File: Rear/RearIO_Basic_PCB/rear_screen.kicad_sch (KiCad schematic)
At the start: 46 parts, among them J1 Conn_01x02_Pin, J2 Conn_01x02_Pin, J3 Conn_01x02_Pin, J4 Conn_01x02_Pin, J5 Conn_01x02_Pin, J6 Conn_01x02_Pin, J7 Conn_01x08_Socket, Q1 NTMFS4C03N-HXY, Q2 NTMFS4C03N-HXY, Q3 NTMFS4C03N-HXY, Q4 NTMFS4C03N-HXY, Q6 NTMFS4C03N-HXY, Q7 NTMFS4C03N-HXY, U1 MIC4426, U2 MIC4426, U3 AOZ1280CI, U4 ACS711xEXLT-31AB

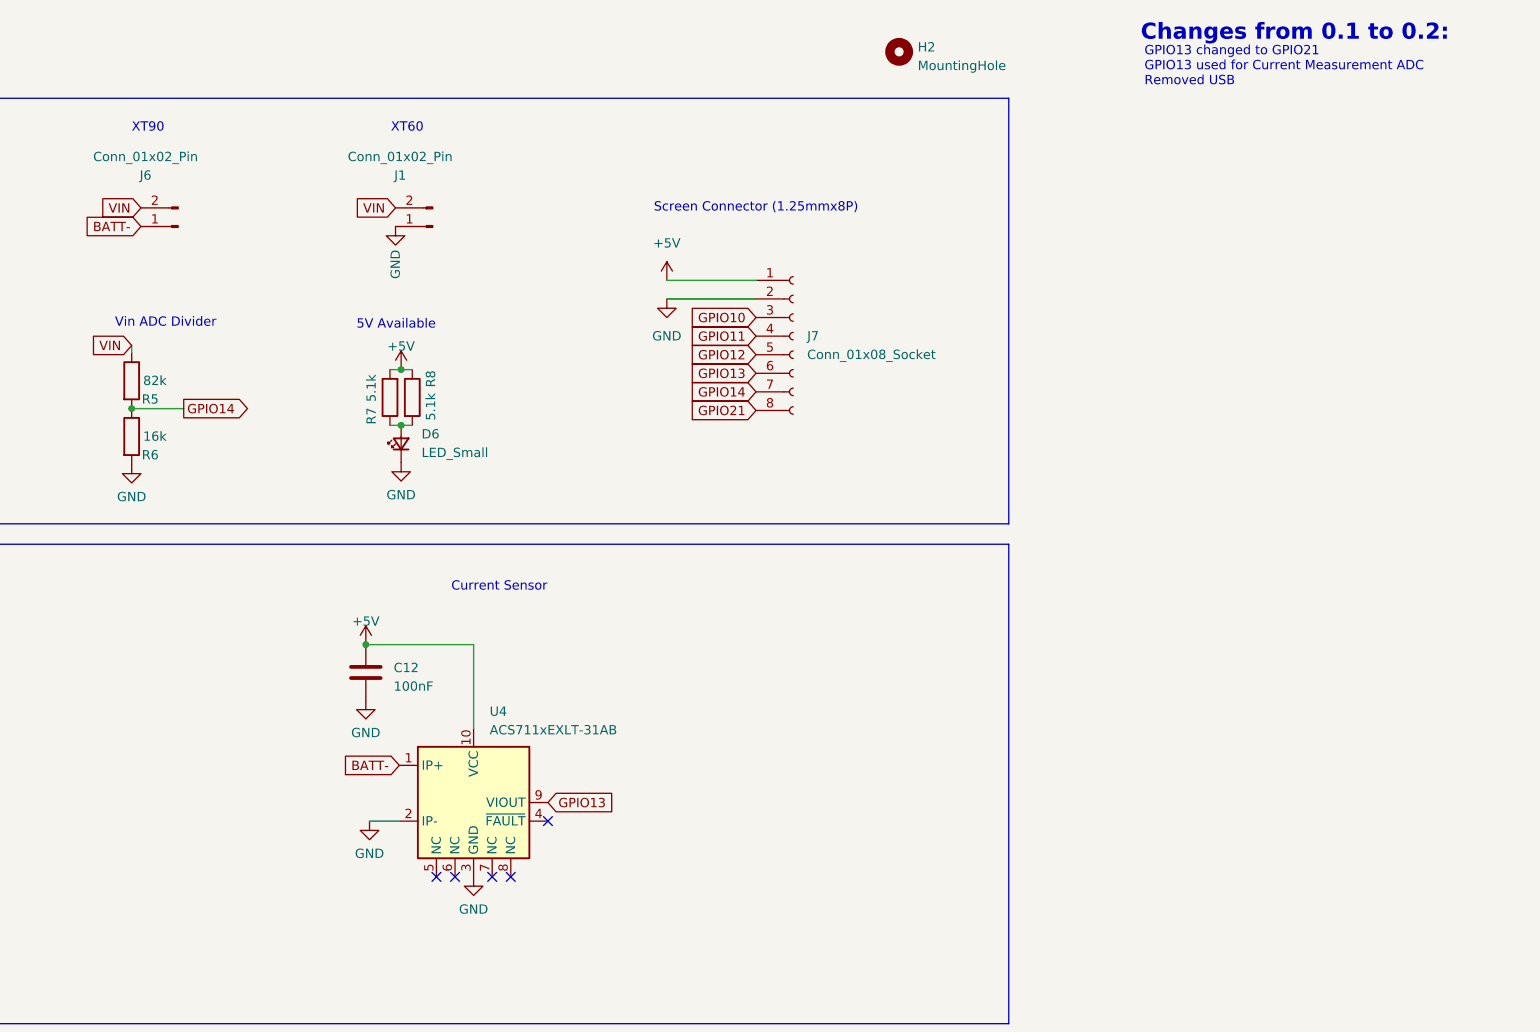
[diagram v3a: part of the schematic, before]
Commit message: v0.2 submitted to JLCPCB
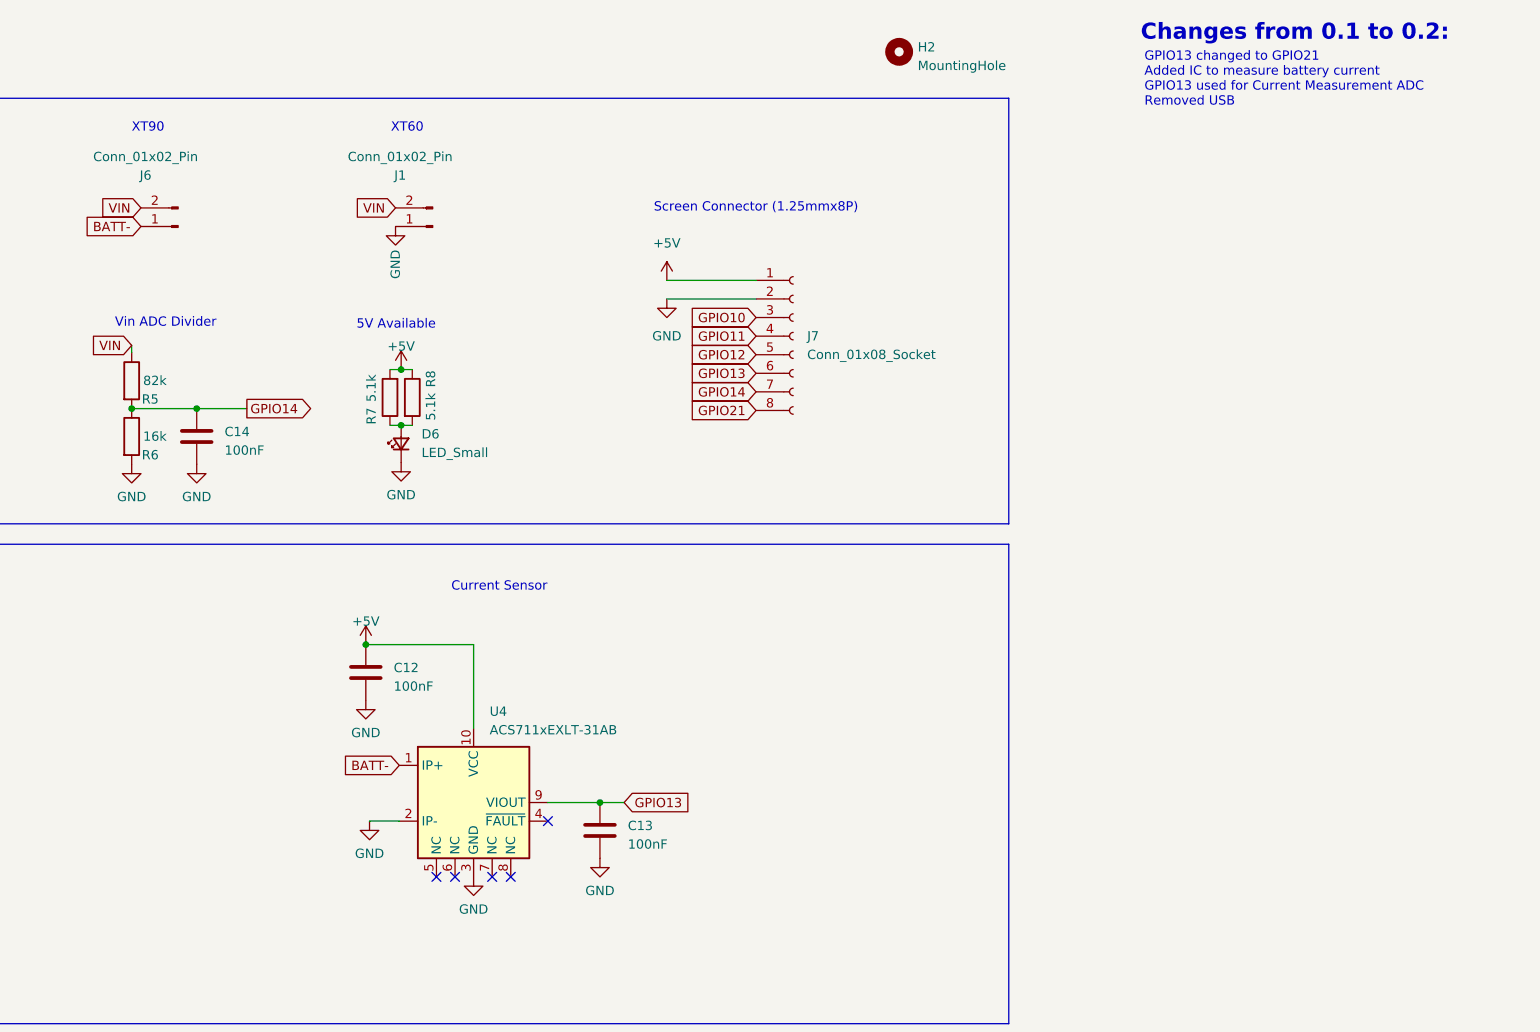
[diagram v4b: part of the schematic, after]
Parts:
- added C13, C14: 100nF, Capacitor_SMD:C_0603_1608Metric, symbol Device:C
- C1: lcsc C99836 -> C340768
- U4: lcsc (none) -> C146412
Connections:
- net GND: now also C13.2, C14.2
- net GPIO13: now also C13.1
- net GPIO14: now also C14.1
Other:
- note added: "GPIO13 changed to GPIO21 Added IC to measure battery current GPIO13 used for Current Measurement ADC Removed USB"
- note removed: "GPIO13 changed to GPIO21 GPIO13 used for Current Measurement ADC Removed USB"
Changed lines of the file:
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@@
   (title_block
     (title "Rear-IO:Basic")
-    (date "2023-08-19")
-    (rev "v0.1")
+    (date "2023-09-08")
+    (rev "v0.2")
     (company "Ace's Electronics")
   )
@@
   (junction (at 90.424 43.561) (diameter 0) (color 0 0 0 0)
   )
+  (junction (at 226.06 117.856) (diameter 0) (color 0 0 0 0)
+  )
   (junction (at 162.052 64.008) (diameter 0) (color 0 0 0 0)
   )
@@
   )
   (junction (at 35.179 35.941) (diameter 0) (color 0 0 0 0)
+  )
+  (junction (at 170.942 64.008) (diameter 0) (color 0 0 0 0)
   )
   (junction (at 163.068 170.053) (diameter 0) (color 0 0 0 0)
@@
     (stroke (width 0) (type default))
   )
-  (wire (pts (xy 162.052 64.008) (xy 169.164 64.008))
+  (wire (pts (xy 162.052 64.008) (xy 170.942 64.008))
     (stroke (width 0) (type default))
   )
@@
     (stroke (width 0) (type default))
   )
+  (wire (pts (xy 226.06 117.856) (xy 218.948 117.856))
+    (stroke (width 0) (type default))
+  )
   (wire (pts (xy 235.204 49.022) (xy 247.396 49.022))
     (stroke (width 0) (type default))
@@
     (stroke (width 0) (type default))
   )
+  (wire (pts (xy 170.942 64.008) (xy 177.8 64.008))
+    (stroke (width 0) (type default))
+  )
   (wire (pts (xy 90.678 185.293) (xy 117.348 185.293))
     (stroke (width 0) (type default))
@@
   )
   (wire (pts (xy 96.774 84.201) (xy 90.424 84.201))
+    (stroke (width 0) (type default))
+  )
+  (wire (pts (xy 229.362 117.856) (xy 226.06 117.856))
     (stroke (width 0) (type default))
   )
@@
     (effects (font (size 1.27 1.27)) (justify left bottom))
   )
-  (text "GPIO13 changed to GPIO21\nGPIO13 used for Current Measurement ADC\nRemoved USB"
-    (at 300.482 20.066 0)
+  (text "GPIO13 changed to GPIO21\nAdded IC to measure battery current\nGPIO13 used for Current Measurement ADC\nRemoved USB"
+    (at 300.482 22.86 0)
     (effects (font (size 1.27 1.27)) (justify left bottom))
   )
@@
     )
   )
-  (global_label "GPIO14" (shape output) (at 169.164 64.008 0) (fields_autoplaced)
+  (global_label "GPIO14" (shape output) (at 177.8 64.008 0) (fields_autoplaced)
     (effects (font (size 1.27 1.27)) (justify left))
-    (property "Intersheetrefs" "${INTERSHEET_REFS}" (at 179.0435 64.008 0)
+    (property "Intersheetrefs" "${INTERSHEET_REFS}" (at 187.6795 64.008 0)
       (effects (font (size 1.27 1.27)) (justify left) hide)
     )
@@
     )
   )
-  (global_label "GPIO13" (shape input) (at 218.948 117.856 0) (fields_autoplaced)
+  (global_label "GPIO13" (shape input) (at 229.362 117.856 0) (fields_autoplaced)
     (effects (font (size 1.27 1.27)) (justify left))
-    (property "Intersheetrefs" "${INTERSHEET_REFS}" (at 228.8275 117.856 0)
+    (property "Intersheetrefs" "${INTERSHEET_REFS}" (at 239.2415 117.856 0)
       (effects (font (size 1.27 1.27)) (justify left) hide)
     )
@@
     )
   )
+  (symbol (lib_id "power:GND") (at 170.942 71.628 0) (unit 1)
+    (in_bom yes) (on_board yes) (dnp no) (fields_autoplaced)
+    (property "Reference" "#PWR034" (at 170.942 77.978 0)
+      (effects (font (size 1.27 1.27)) hide)
+    )
+    (property "Value" "GND" (at 170.942 76.073 0)
+      (effects (font (size 1.27 1.27)))
+    )
+    (property "Footprint" "" (at 170.942 71.628 0)
+      (effects (font (size 1.27 1.27)) hide)
+    )
+    (property "Datasheet" "" (at 170.942 71.628 0)
+      (effects (font (size 1.27 1.27)) hide)
+    )
+    (pin "1")
+    (instances
+      (project "rear_screen"
+        (path "/910a7c84-921d-4524-a88f-3df0134676d0"
+          (reference "#PWR034") (unit 1)
+        )
+      )
+      (project "rev1"
+        (path "/996d0415-70c6-48f9-916e-4dbf0ceb94fa"
+          (reference "#PWR031") (unit 1)
+        )
+      )
+    )
+  )
   (symbol (lib_id "Sensor_Current:ACS711xEXLT-31AB") (at 208.788 117.856 0) (unit 1)
     (in_bom yes) (on_board yes) (dnp no) (fields_autoplaced)
@@
     )
     (property "Datasheet" "http://www.allegromicro.com/~/Media/Files/Datasheets/ACS711-Datasheet.ashx" (at 208.788 117.856 0)
+      (effects (font (size 1.27 1.27)) hide)
+    )
+    (property "lcsc" "C146412" (at 208.788 117.856 0)
       (effects (font (size 1.27 1.27)) hide)
     )
@@
     )
   )
+  (symbol (lib_id "Device:C") (at 226.06 121.666 0) (unit 1)
+    (in_bom yes) (on_board yes) (dnp no) (fields_autoplaced)
+    (property "Reference" "C13" (at 229.87 121.031 0)
+      (effects (font (size 1.27 1.27)) (justify left))
+    )
+    (property "Value" "100nF" (at 229.87 123.571 0)
+      (effects (font (size 1.27 1.27)) (justify left))
+    )
+    (property "Footprint" "Capacitor_SMD:C_0603_1608Metric" (at 227.0252 125.476 0)
+      (effects (font (size 1.27 1.27)) hide)
+    )
+    (property "Datasheet" "~" (at 226.06 121.666 0)
+      (effects (font (size 1.27 1.27)) hide)
+    )
+    (property "lcsc" "C30926" (at 226.06 121.666 0)
+      (effects (font (size 1.27 1.27)) hide)
+    )
+    (pin "1")
+    (pin "2")
+    (instances
+      (project "rear_screen"
+        (path "/910a7c84-921d-4524-a88f-3df0134676d0"
+          (reference "C13") (unit 1)
+        )
+      )
+    )
+  )
   (symbol (lib_id "Device:C") (at 97.028 166.243 0) (unit 1)
     (in_bom yes) (on_board yes) (dnp no) (fields_autoplaced)
@@
       (effects (font (size 1.27 1.27)) hide)
     )
-    (property "lcsc" "C99836" (at 24.638 171.323 0)
+    (property "lcsc" "C340768" (at 24.638 171.323 0)
       (effects (font (size 1.27 1.27)) hide)
     )
@@
         (path "/910a7c84-921d-4524-a88f-3df0134676d0"
           (reference "C3") (unit 1)
+        )
+      )
+    )
+  )
+  (symbol (lib_id "power:GND") (at 226.06 125.476 0) (unit 1)
+    (in_bom yes) (on_board yes) (dnp no) (fields_autoplaced)
+    (property "Reference" "#PWR033" (at 226.06 131.826 0)
+      (effects (font (size 1.27 1.27)) hide)
+    )
+    (property "Value" "GND" (at 226.06 129.921 0)
+      (effects (font (size 1.27 1.27)))
+    )
+    (property "Footprint" "" (at 226.06 125.476 0)
+      (effects (font (size 1.27 1.27)) hide)
+    )
+    (property "Datasheet" "" (at 226.06 125.476 0)
+      (effects (font (size 1.27 1.27)) hide)
+    )
+    (pin "1")
+    (instances
+      (project "rear_screen"
+        (path "/910a7c84-921d-4524-a88f-3df0134676d0"
+          (reference "#PWR033") (unit 1)
+        )
+      )
+      (project "rev1"
+        (path "/996d0415-70c6-48f9-916e-4dbf0ceb94fa"
+          (reference "#PWR031") (unit 1)
         )
       )
@@
         )
       )
+    )
+  )
+  (symbol (lib_id "Device:C") (at 170.942 67.818 0) (unit 1)
+    (in_bom yes) (on_board yes) (dnp no) (fields_autoplaced)
+    (property "Reference" "C14" (at 174.752 67.183 0)
+      (effects (font (size 1.27 1.27)) (justify left))
+    )
+    (property "Value" "100nF" (at 174.752 69.723 0)
+      (effects (font (size 1.27 1.27)) (justify left))
+    )
+    (property "Footprint" "Capacitor_SMD:C_0603_1608Metric" (at 171.9072 71.628 0)
+      (effects (font (size 1.27 1.27)) hide)
+    )
+    (property "Datasheet" "~" (at 170.942 67.818 0)
+      (effects (font (size 1.27 1.27)) hide)
+    )
+    (property "lcsc" "C30926" (at 170.942 67.818 0)
+      (effects (font (size 1.27 1.27)) hide)
+    )
+    (pin "1")
+    (pin "2")
+    (instances
+      (project "rear_screen"
+        (path "/910a7c84-921d-4524-a88f-3df0134676d0"
+          (reference "C14") (unit 1)
+        )
+      )

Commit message: WIP
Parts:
- removed C10, C8: 10uF, Capacitor_SMD:C_0603_1608Metric, symbol Device:C
- removed C11, C9: 100nF, Capacitor_SMD:C_0603_1608Metric, symbol Device:C
- removed R7: 5.1k, Resistor_SMD:R_0603_1608Metric, symbol Device:R
- removed U1, U2: MIC4426, Package_SO:HSOP-8-1EP_3.9x4.9mm_P1.27mm_EP2.41x3.1mm_ThermalVias, symbol Driver_FET:MIC4426
- added D1, D8: CI20S120M3, Package_TO_SOT_SMD:TO-263-2_TabPin1, symbol Diode:C3D06060G
- added Q10, Q5, Q8, Q9: MMBT3904, Package_TO_SOT_SMD:SOT-23, symbol Transistor_BJT:MMBT3904
- added R1, R10, R12, R9: 1k, Resistor_SMD:R_0603_1608Metric, symbol Device:R
- added R11, R13, R14, R2: 16k, Resistor_SMD:R_0603_1608Metric, symbol Device:R
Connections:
- net BATT-: now also J1.1 (Pin_1)
- net GND: now also Q10.2 (E), Q5.2 (E), Q8.2 (E), Q9.2 (E); no longer J1.1 (Pin_1)
- net GPIO10: now also R1.1
- net GPIO11: now also R9.1
- net GPIO12: now also R10.1
- net GPIO21: now also R12.1
- net at Q1.4 (G), Q2.4 (G): now also Q5.3 (C), R11.2
- net at Q7.4 (G): now also Q10.3 (C), R14.2
- net at Q6.4 (G): now also Q9.3 (C), R13.2
- net at Q3.4 (G), Q4.4 (G): now also Q8.3 (C), R2.2
- net VIN renamed +BATT
- net +BATT: now also D1.1 (K), D8.1 (K), R11.1, R13.1, R14.1, R2.1; no longer J1.2 (Pin_2), J6.2 (Pin_2)
- new net: Q5.1 (B), R1.2
- new net: Q9.1 (B), R10.2
- new net: D1.2 (A), J1.2 (Pin_2)
- new net: D8.2 (A), J6.2 (Pin_2)
- new net: Q10.1 (B), R12.2
- new net: Q8.1 (B), R9.2
- no-connect marks 7 -> 5
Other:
- note added: "Batt ADC Divider"
- note added: "Changes from 0.2 to 0.3:"
- note added: "Swapped out Mosfet Driver ICs for BJTs Added Solar and 12V inputs, through diodes Physically swapped the HP2 and LP1 positions on the PCB"
- note added: "XT60 - Solar Out"
- note added: "XT90 - Vehicle 12V"
- note removed: "Vin ADC Divider"
- note removed: "XT60"
- note removed: "XT90"
- moved on the sheet: C12, C13, D2, D3, D4, D5, J2, J3, J4, J5, J7, Q6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

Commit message: Started work on v0.3 software
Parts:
- removed C13, C14: 100nF, Capacitor_SMD:C_0603_1608Metric, symbol Device:C
- removed D1, D8: CI20S120M3, Package_TO_SOT_SMD:TO-263-2_TabPin1, symbol Diode:C3D06060G
- removed D2: 1N5819WS, Diode_SMD:D_SOD-323, symbol Diode:1N5819WS
- removed Q10: MMBT3904, Package_TO_SOT_SMD:SOT-23, symbol Transistor_BJT:MMBT3904
- removed Q7: NTMFS4C03N-HXY, Package_TO_SOT_SMD:LFPAK56, symbol Transistor_FET:PSMN5R2-60YL
- removed R5: 82k, Resistor_SMD:R_0603_1608Metric, symbol Device:R
- removed U4: ACS711xEXLT-31AB, Sensor_Current:Allegro_QFN-12-10-1EP_3x3mm_P0.5mm, symbol Sensor_Current:ACS711xEXLT-31AB
- added C8, C9: 100nF, Capacitor_SMD:C_0603_1608Metric, symbol Device:C
- added J10: Conn_01x02_Pin, Acea:AMASS_XT90PW-M, symbol Connector:Conn_01x02_Pin
- added J11: Conn_01x02_Pin, Connector_AMASS:AMASS_XT60PW-F_1x02_P7.20mm_Horizontal, symbol Connector:Conn_01x02_Pin
- added J9: Conn_01x02_Pin, Connector_AMASS:AMASS_XT60PW-M_1x02_P7.20mm_Horizontal, symbol Connector:Conn_01x02_Pin
- added Q10, Q13, Q16, Q7: AON6411, Acea:PowerDI5060-8, symbol Transistor_FET:AON6411
- added Q11: NTMFS4C03N-HXY, Package_TO_SOT_SMD:LFPAK56, symbol Transistor_FET:PSMN5R2-60YL
- added R15, R7: 10mR, Acea:2728R_C500749, symbol Device:R
- added R16: 2k, Resistor_SMD:R_0603_1608Metric, symbol Device:R
- added R18, R20: 16k, Resistor_SMD:R_0603_1608Metric, symbol Device:R
- added U2, U4, U5: INA236AIDDFR_C5443912, Package_TO_SOT_SMD:SOT-23-8, symbol INA236AIDDFR_C5443912:INA236AIDDFR_C5443912
- J1: footprint Connector_AMASS:AMASS_XT60PW-M_1x02_P7.20mm_Horizontal -> Connector_AMASS:AMASS_XT60PW-F_1x02_P7.20mm_Horizontal; lcsc C98732 -> C428722
- J2: footprint Connector_AMASS:AMASS_XT60PW-F_1x02_P7.20mm_Horizontal -> Connector_AMASS:AMASS_XT60PW-M_1x02_P7.20mm_Horizontal; lcsc C428722 -> C98732
- R12: value 1k -> 10mR; footprint Resistor_SMD:R_0603_1608Metric -> Acea:2728R_C500749; lcsc C21190 -> C500749
- R14: value 16k -> 2k; lcsc C4210 -> C22975
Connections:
- net +5V: now also R14.2, C8.1, C9.1, R16.2, U2.4 (VS), U2.7 (A0), U4.4 (VS), U5.4 (VS)
- net +BATT: now also R12.2, J9.2 (Pin_2), U4.1 (IN+); no longer J2.2 (Pin_2), R14.1
- net GND: now also J1.2 (Pin_2), J2.1 (Pin_1), J6.1 (Pin_1), C8.2, C9.2, J10.2 (Pin_2), J11.2 (Pin_2), J9.1 (Pin_1), Q11.1 (S), Q11.2 (S), Q11.3 (S), U2.3 (GND), U4.3 (GND), U5.3 (GND), U5.7 (A0); no longer R6.2
- net GPIO13: now also R14.1, U2.6 (SDA), U4.6 (SDA), U4.7 (A0), U5.6 (SDA)
- net GPIO14: now also R16.1, U2.5 (SCL), U4.5 (SCL), U5.5 (SCL); no longer R6.1
- net GPIO21: no longer R12.1
- net at Q6.4 (G), Q9.3 (C), R13.2: now also Q11.4 (G)
- net V: now reaches J6.2 (Pin_2)
- net V: now also Q16.1 (S), Q16.2 (S), Q16.3 (S), R20.1
- net at D3.2 (A), J3.1 (Pin_1), Q6.5 (D): now also Q11.5 (D)
- net BATT- renamed S-
- net S-: now also R15.1, U2.2 (IN-); no longer J6.1 (Pin_1)
- new net ABFET: Q10.4 (G), Q7.4 (G), R6.2, U4.8 (ALRT)
- new net ASFET: Q13.4 (G), R18.2, U2.8 (ALRT)
- new net AVFET: Q16.4 (G), R20.2, U5.8 (ALRT)
- new net B: J10.1 (Pin_1), Q10.1 (S), Q10.2 (S), Q10.3 (S), Q7.1 (S), Q7.2 (S), Q7.3 (S), R6.1
- new net B-: Q10.5 (D), Q7.5 (D), R12.1, U4.2 (IN-)
- new net S: J2.2 (Pin_2), Q13.1 (S), Q13.2 (S), Q13.3 (S), R18.1
- new net S+: Q13.5 (D), R15.2, U2.1 (IN+)
- new net V+: Q16.5 (D), R7.2, U5.1 (IN+)
- new net V-: J11.1 (Pin_1), R7.1, U5.2 (IN-)
- no-connect marks 5 -> 0
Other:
- note added: "Battery I and V Sensor"
- note added: "Battery Passthrough"
- note added: "Battery Safety Switch"
- note added: "Battery Switch Junction Temps: @21A,147C/150C Max."
- note added: "Changes from 0.3 to 0.4:"
- note added: "I2C Pull-ups"
- note added: "I2C:0x40"
- note added: "I2C:0x41"
- note added: "I2C:0x42"
- note added: "IN"
- note added: "Load Switch (Outputs)Junction Temps: @39A,149C/150C Max."
- note added: "Modified PCB edge to better fit the reset button"
- note added: "Notes to self: Add a low IQ 3.3V LDO Move PAneL LCD HoLe doWn 3mm"
- note added: "OUT"
- note added: "Output 1"
- note added: "Output 2"
- note added: "Output 3"
- note added: "Removed an output Removed analog current and voltage monitor Changed out Mosfet Driver ICs for BJTs Changed all outputs to high current Added Solar and 12V inputs, through diodes Added I2C Added GPIO expander Added I2C current and voltage measurement x3 Added MOSFETs to act as digital fuses"
- note added: "SCL"
- note added: "SDA"
- note added: "SPARE"
- note added: "Solar I and V Sensor"
- note added: "Solar Passthrough"
- note added: "Solar Safety Switch"
- note added: "Thermals"
- note added: "Vehicle 12V I and V Sensor"
- note added: "Vehicle 12V Passthrough"
- note added: "Vehicle Safety Switch"
- note added: "eFuse set at 20A"
- note removed: "Batt ADC Divider"
- note removed: "Current Sensor"
- note removed: "Lower Current IO"
- note removed: "Port HP1"
- note removed: "Port HP2"
- note removed: "Port LP1"
- note removed: "Port LP2"
- note removed: "Swapped out Mosfet Driver ICs for BJTs Added Solar and 12V inputs, through diodes Physically swapped the HP2 and LP1 positions on the PCB"
- note removed: "XT60 - Solar Out"
- note removed: "XT90 - Vehicle 12V"
- moved on the sheet: C1, C12, C2, C3, C4, C5, C6, C7, D3, D4, D5, D6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

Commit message: Final UI changes
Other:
- note added: "Make the pins go 1 to 1 swap GND and 12V"
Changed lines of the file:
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@@
+		)
+	)
+	(text "Make the pins go 1 to 1\nswap GND and 12V"
+		(exclude_from_sim no)
+		(at 274.828 143.002 0)
+		(effects
+			(font
+				(size 2.2 2.2)
+				(thickness 0.44)
+				(bold yes)
+			)
+			(justify left bottom)
 		)
 	)
